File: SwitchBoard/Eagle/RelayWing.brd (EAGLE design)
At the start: 51.7 x 55.9 mm, 29 parts, among them K1 EE2-3TNUH, K2 EE2-3TNUH, K3 EE2-3TNUH, K4 EE2-3TNUH, K5 EE2-3TNUH, U1 ULN2003ANS, U2 ULN2003ANS, U3 MCP23017SS, U4 INA219AID

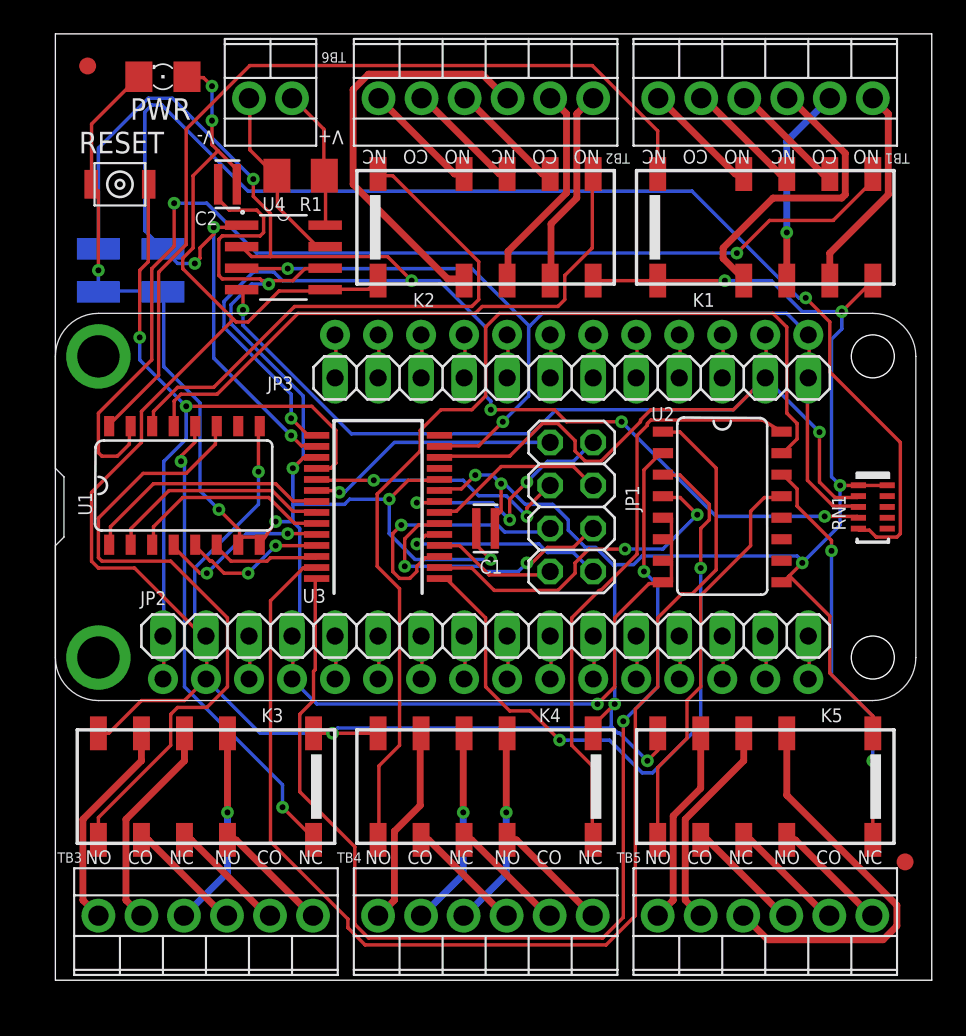
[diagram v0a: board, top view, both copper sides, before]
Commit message: Fix contact labels.
Moved relays, labeled between pads. Cleaned up schematic around R1. Reviewed schematic and board. Design rules pass except around left mounting holes.
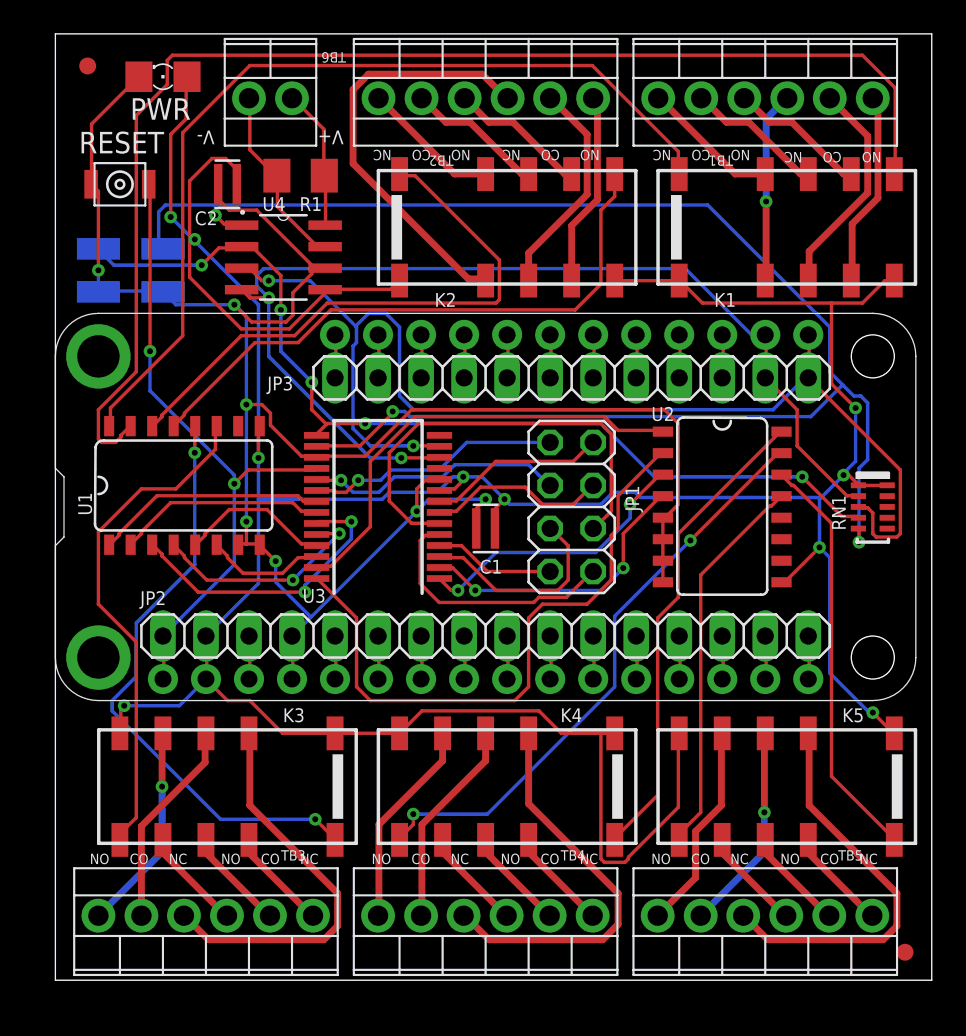
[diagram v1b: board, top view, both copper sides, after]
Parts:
- moved U$3 5.33 mm to (50.2, 15.6)
- moved K1 1.27 mm to (43.2, 58.4)
- moved K2 1.27 mm to (26.7, 58.4)
- moved K4 1.27 mm to (26.7, 25.4)
- moved K5 1.27 mm to (43.2, 25.4)
- moved K3 1.27 mm to (10.2, 25.4)
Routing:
- net N$68: track 75.6 -> 26.8 mm
- net A0: track 91.5 -> 56.9 mm, vias 6 -> 5
- net N$69: track 68.8 -> 37.0 mm, vias 2 -> 0
- net N$59: track 62.4 -> 34.9 mm, vias 0 -> 2
- net N$70: track 40.4 -> 16.8 mm
- net GND: track 140.5 -> 121.5 mm, vias 8 -> 7
- net SDA: track 58.6 -> 70.4 mm
- net N$53: track 11.8 -> 23.5 mm, vias 1 -> 0
- net N$79: track 11.9 -> 23.6 mm, vias 1 -> 0
- net N$34: track 64.5 -> 75.5 mm, vias 2 -> 0
- net N$75: track 16.4 -> 26.5 mm, vias 2 -> 0
- net SCL: track 73.2 -> 63.5 mm
- net N$39: track 38.5 -> 29.8 mm
- net N$38: track 28.0 -> 35.2 mm
- net N$58: track 35.2 -> 28.2 mm
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
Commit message: Fix Ax pads, rear text.
Added bRestrict & vRestrict to address pads to keep vias & traces out of cut area. Added new shorted jumper device to prevent routing to GND via Ax. If problems, route w/ SJW then replace w/ SJW-SHORTED.

Added bottom text.
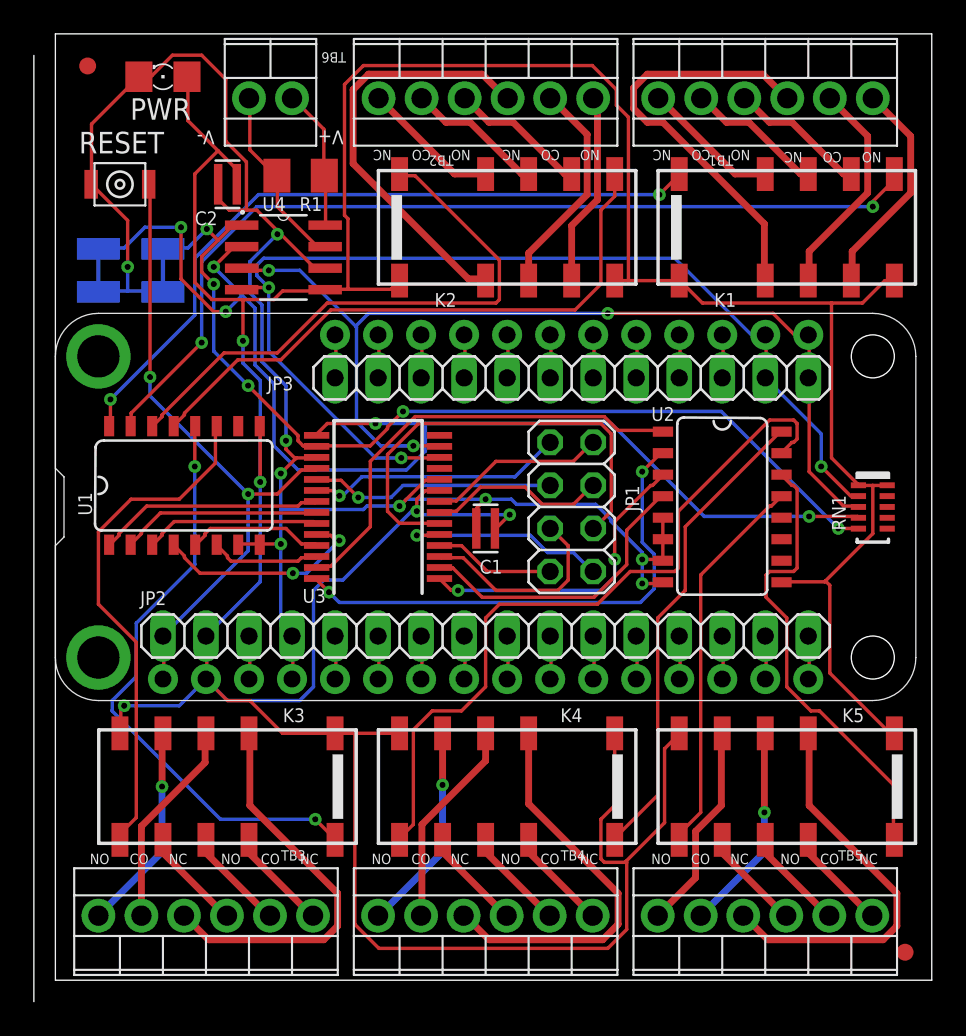
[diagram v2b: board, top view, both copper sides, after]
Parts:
- A0, A1: device jumper:SJW -> home:SJW-SHORTED
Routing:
- net 3V: track 209.8 -> 248.8 mm, vias 10 -> 5
- net A1: track 95.3 -> 57.4 mm, vias 3 -> 5
- net N$34: track 75.5 -> 54.9 mm, vias 0 -> 2
- net A0: track 56.9 -> 73.7 mm
- net N$28: track 11.3 -> 25.1 mm, vias 1 -> 0
- net GND: track 121.5 -> 109.6 mm, vias 7 -> 9
- net SDA: track 70.4 -> 58.8 mm, vias 2 -> 3
- net N$24: track 53.5 -> 42.7 mm, vias 0 -> 2
- net N$59: track 34.9 -> 43.7 mm, vias 2 -> 0
- net N$64: track 17.6 -> 10.4 mm, vias 2 -> 0
- net N$69: track 37.0 -> 29.8 mm, vias 0 -> 2
- net N$60: track 24.4 -> 27.0 mm
- net N$74: track 15.3 -> 12.7 mm, vias 0 -> 1
- net N$16: track 11.5 -> 13.1 mm
- net N$70: track 16.8 -> 18.2 mm
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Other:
- board size 51.7 x 55.9 mm -> 53 x 57.1 mm
- board text added: "ATMakers"
- board text added: "Current Monitor & IO Exp Address"
- board text added: "SwitchBoard Rev. A 26V, 2A MAX"

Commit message: Move text off vias, rm copied dim line.
vRestrict ares for labels were lost. Re-apply on re-route.
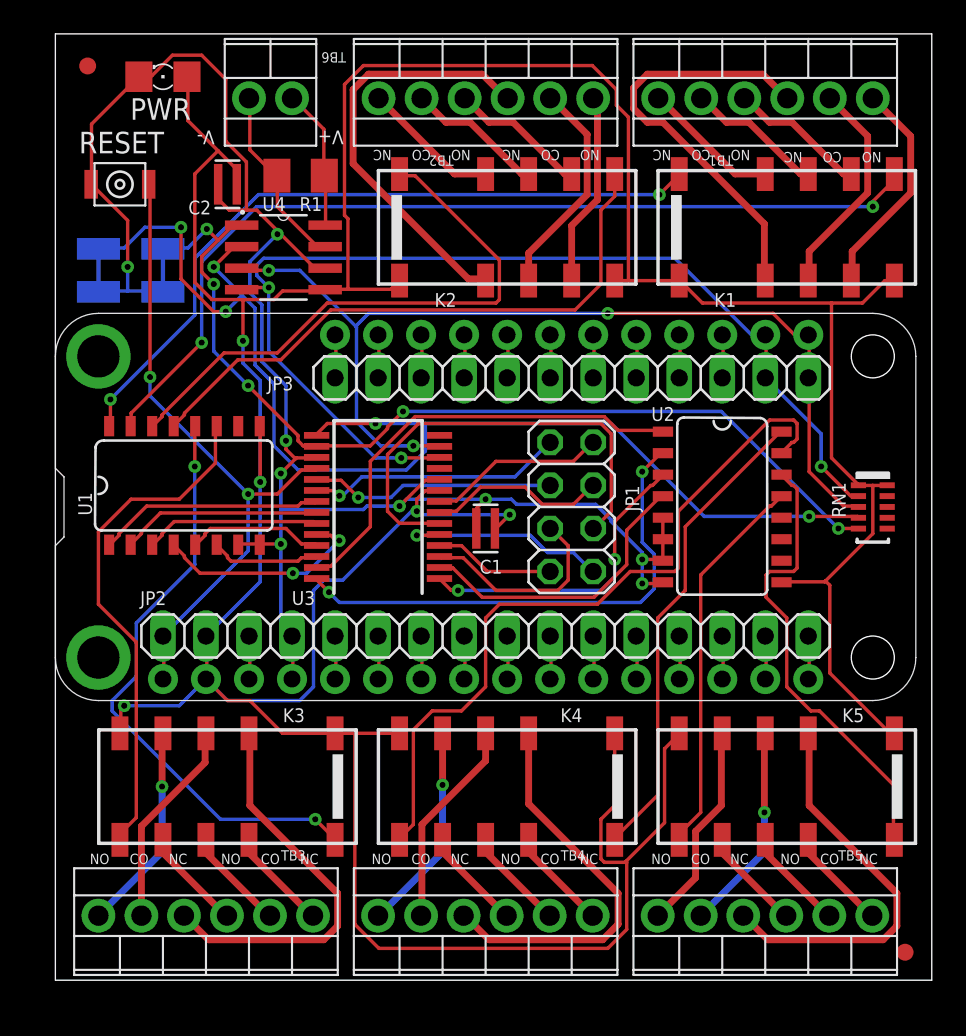
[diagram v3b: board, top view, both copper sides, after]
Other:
- board size 53 x 57.1 mm -> 51.7 x 55.9 mm
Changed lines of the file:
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@@
 <grid distance="50" unitdist="mil" unit="mil" style="lines" multiple="1" display="yes" altdistance="5" altunitdist="mil" altunit="mil"/>
 <layers>
-<layer number="1" name="Top" color="4" fill="1" visible="yes" active="yes"/>
-<layer number="2" name="Route2" color="1" fill="3" visible="yes" active="yes"/>
-<layer number="15" name="Route15" color="4" fill="6" visible="yes" active="yes"/>
-<layer number="16" name="Bottom" color="1" fill="1" visible="yes" active="yes"/>
+<layer number="1" name="Top" color="4" fill="1" visible="no" active="yes"/>
+<layer number="2" name="Route2" color="1" fill="3" visible="no" active="yes"/>
+<layer number="15" name="Route15" color="4" fill="6" visible="no" active="yes"/>
+<layer number="16" name="Bottom" color="1" fill="1" visible="no" active="yes"/>
 <layer number="17" name="Pads" color="2" fill="1" visible="yes" active="yes"/>
 <layer number="18" name="Vias" color="2" fill="1" visible="yes" active="yes"/>
@@
 <layer number="20" name="Dimension" color="24" fill="1" visible="yes" active="yes"/>
 <layer number="21" name="tPlace" color="7" fill="1" visible="yes" active="yes"/>
-<layer number="22" name="bPlace" color="24" fill="1" visible="yes" active="yes"/>
+<layer number="22" name="bPlace" color="24" fill="1" visible="no" active="yes"/>
 <layer number="23" name="tOrigins" color="15" fill="1" visible="yes" active="yes"/>
-<layer number="24" name="bOrigins" color="15" fill="1" visible="yes" active="yes"/>
+<layer number="24" name="bOrigins" color="15" fill="1" visible="no" active="yes"/>
 <layer number="25" name="tNames" color="7" fill="1" visible="yes" active="yes"/>
-<layer number="26" name="bNames" color="7" fill="1" visible="yes" active="yes"/>
-<layer number="27" name="tValues" color="7" fill="1" visible="yes" active="yes"/>
-<layer number="28" name="bValues" color="7" fill="1" visible="yes" active="yes"/>
-<layer number="29" name="tStop" color="7" fill="3" visible="no" active="yes"/>
+<layer number="26" name="bNames" color="7" fill="1" visible="no" active="yes"/>
+<layer number="27" name="tValues" color="7" fill="1" visible="no" active="yes"/>
+<layer number="28" name="bValues" color="7" fill="1" visible="no" active="yes"/>
+<layer number="29" name="tStop" color="7" fill="3" visible="yes" active="yes"/>
 <layer number="30" name="bStop" color="7" fill="6" visible="no" active="yes"/>
-<layer number="31" name="tCream" color="7" fill="4" visible="no" active="yes"/>
+<layer number="31" name="tCream" color="7" fill="4" visible="yes" active="yes"/>
 <layer number="32" name="bCream" color="7" fill="5" visible="no" active="yes"/>
 <layer number="33" name="tFinish" color="6" fill="3" visible="no" active="yes"/>
@@
 <layer number="38" name="bTest" color="7" fill="1" visible="no" active="yes"/>
 <layer number="39" name="tKeepout" color="4" fill="11" visible="yes" active="yes"/>
-<layer number="40" name="bKeepout" color="1" fill="11" visible="yes" active="yes"/>
+<layer number="40" name="bKeepout" color="1" fill="11" visible="no" active="yes"/>
 <layer number="41" name="tRestrict" color="4" fill="10" visible="yes" active="yes"/>
-<layer number="42" name="bRestrict" color="1" fill="10" visible="yes" active="yes"/>
+<layer number="42" name="bRestrict" color="1" fill="10" visible="no" active="yes"/>
 <layer number="43" name="vRestrict" color="2" fill="10" visible="no" active="yes"/>
-<layer number="44" name="Drills" color="7" fill="1" visible="yes" active="yes"/>
+<layer number="44" name="Drills" color="7" fill="1" visible="no" active="yes"/>
 <layer number="45" name="Holes" color="7" fill="1" visible="yes" active="yes"/>
 <layer number="46" name="Milling" color="3" fill="1" visible="no" active="yes"/>
@@
 <layer number="50" name="dxf" color="7" fill="1" visible="no" active="no"/>
 <layer number="51" name="tDocu" color="7" fill="1" visible="yes" active="yes"/>
-<layer number="52" name="bDocu" color="7" fill="1" visible="yes" active="yes"/>
+<layer number="52" name="bDocu" color="7" fill="1" visible="no" active="yes"/>
 <layer number="53" name="tGND_GNDA" color="7" fill="9" visible="no" active="no"/>
 <layer number="54" name="bGND_GNDA" color="1" fill="9" visible="no" active="no"/>
@@
 <rectangle x1="1.27" y1="55.245" x2="3.81" y2="56.515" layer="43"/>
 <rectangle x1="5.08" y1="55.245" x2="7.62" y2="56.515" layer="43"/>
-<wire x1="-1.27" y1="68.57" x2="-1.27" y2="12.7" width="0" layer="20"/>
 <rectangle x1="6.731" y1="55.245" x2="7.239" y2="56.515" layer="42"/>
 <rectangle x1="2.921" y1="55.245" x2="3.429" y2="56.515" layer="42"/>
@@
 </element>
 <element name="C2" library="home" package="CAPC2012" value="MUR-1220-CAP" x="10.16" y="60.96" smashed="yes">
-<attribute name="NAME" x="8.2296" y="58.547" size="0.8128" layer="25" ratio="10" rot="SR0"/>
+<attribute name="NAME" x="7.8486" y="59.182" size="0.8128" layer="25" ratio="10" rot="SR0"/>
 </element>
 <element name="K1" library="home" package="NUH" value="EE2-3TNUH" x="43.18" y="58.42" smashed="yes">
@@
 <attribute name="MF" value="MICROCHIP" x="19.05" y="41.91" size="1.778" layer="27" rot="R90" display="off"/>
 <attribute name="MPN" value="MCP23017-E/SS" x="19.05" y="41.91" size="1.778" layer="27" rot="R90" display="off"/>
-<attribute name="NAME" x="15.9649" y="37.069" size="0.8128" layer="25" rot="R180"/>
+<attribute name="NAME" x="15.3299" y="36.942" size="0.8128" layer="25" rot="R180"/>
 <attribute name="OC_FARNELL" value="1467674" x="19.05" y="41.91" size="1.778" layer="27" rot="R90" display="off"/>
 <attribute name="OC_NEWARK" value="31K2960" x="19.05" y="41.91" size="1.778" layer="27" rot="R90" display="off"/>
@@
 </element>
 <element name="RN1" library="home" package="CTS746" value="CTS7461011" x="48.26" y="41.91" smashed="yes" rot="R270">
-<attribute name="NAME" x="45.847" y="42.606" size="0.8128" layer="25" rot="R270"/>
+<attribute name="NAME" x="45.847" y="43.368" size="0.8128" layer="25" rot="R270"/>
 <attribute name="VALUE" x="49.784" y="45.288" size="0.8128" layer="27" rot="R270"/>
 </element>
